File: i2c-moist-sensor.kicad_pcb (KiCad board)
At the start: 2 copper layers, 18 x 149 mm, 25 parts, among them IC1 ATTINY441-SSU, P1 CONN_02X03, X1 16MHz

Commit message: SPBTLE version 1.0 - HW
Only hardware changes
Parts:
- removed C2: 33pp, Capacitors_SMD:C_0603
- removed G***: LOGO, w_logo:Logo_silk_OSHW_6x6mm
- removed G***: LOGO, chirp_logo:ziogas
- removed IC1: ATTINY441-SSU, Housings_SOIC:SOIC-14_3.9x8.7mm_Pitch1.27mm
- removed P1: CONN_02X03, Pin_Headers:Pin_Header_Straight_2x03
- removed the REF** at (91.5, 17.0)
- removed the REF** at (98.5, 17.0)
- removed TH1: NCP18XH103F03RB, Resistors_SMD:R_0603
- removed X1: 16MHz, Crystals:Crystal_HC49-SD_SMD
- added C7: 1u, Capacitors_SMD:C_0603_HandSoldering, B.Cu at (52.2, 32.2)
- added D4: LED, LEDs:LED_0603_HandSoldering, F.Cu at (53.2, 58.7)
- added J1: Conn_02x05_Odd_Even, SBenoit:50mils_JTAG, B.Cu at (57.3, 37.4)
- added J2: Conn_01x02, Pin_Headers:Pin_Header_Straight_1x02_Pitch1.27mm, F.Cu at (57.8, 26.2)
- added Q1: BSS83P, TO_SOT_Packages_SMD:SOT-23_Handsoldering, B.Cu at (57.2, 30.0)
- added Q2: RUC002N05HZGT116CT, TO_SOT_Packages_SMD:SOT-23_Handsoldering, B.Cu at (53.2, 45.5)
- added Q3: RUC002N05HZGT116CT, TO_SOT_Packages_SMD:SOT-23_Handsoldering, B.Cu at (53.4, 61.2)
- added Q4: RUC002N05HZGT116CT, TO_SOT_Packages_SMD:SOT-23_Handsoldering, B.Cu at (53.4, 55.0)
- added R10: 100, Resistors_SMD:R_0603_HandSoldering, B.Cu at (52.5, 49.0)
- added R11: 100, Resistors_SMD:R_0603_HandSoldering, B.Cu at (52.5, 63.8)
- added R12: 100, Resistors_SMD:R_0603_HandSoldering, B.Cu at (52.8, 58.0)
- added R3: 1M, Resistors_SMD:R_0603_HandSoldering, F.Cu at (54.8, 67.0)
- added REF**: MountingHole_3.2mm_M3, Mounting_Holes:MountingHole_3.2mm_M3, F.Cu at (50.5, 27.5)
- added REF**: MountingHole_3.2mm_M3, Mounting_Holes:MountingHole_3.2mm_M3, F.Cu at (65.5, 50.0)
- added SW1: SW_Push, Buttons_Switches_SMD:SW_SPST_EVPBF, F.Cu at (58.0, 53.8)
- added U1: SPBTLE-1S, SBenoit:SPBTLE-1s, F.Cu at (58.8, 36.4)
- C1: value 33p -> 330n; footprint Capacitors_SMD:C_0603 -> Capacitors_SMD:C_0603_HandSoldering; moved to B.Cu
- C3: value 1u -> 1n; footprint Capacitors_SMD:C_0603 -> Capacitors_SMD:C_0603_HandSoldering
- C4: value 1n -> 10n; footprint Capacitors_SMD:C_0603 -> Capacitors_SMD:C_0603_HandSoldering
- C5: footprint Capacitors_SMD:C_0603 -> Capacitors_SMD:C_0603_HandSoldering
- C6: value 1u -> 100n; footprint Capacitors_SMD:C_0603 -> Capacitors_SMD:C_0603_HandSoldering; moved to B.Cu
- D3: footprint LEDs:LED-0603 -> LEDs:LED_0603_HandSoldering
- R1: value 10k -> 1M; footprint Resistors_SMD:R_0603 -> Resistors_SMD:R_0603_HandSoldering
- R2: value 10k 0.1% -> 1M; footprint Resistors_SMD:R_0603 -> Resistors_SMD:R_0603_HandSoldering
- R4, R5, R7, R9: footprint Resistors_SMD:R_0603 -> Resistors_SMD:R_0603_HandSoldering
- R6: value 1M -> 47k; footprint Resistors_SMD:R_0603 -> Resistors_SMD:R_0603_HandSoldering; moved to B.Cu
- R8: value 1M -> 330; footprint Resistors_SMD:R_0603 -> Resistors_SMD:R_0603_HandSoldering
- moved D3 52.9 mm to (51.4, 58.7)
- moved R9 49.6 mm to (52.5, 54.2)
- moved R1 49.1 mm to (54.8, 65.2)
- moved C3 47.0 mm to (54.8, 63.5), turned to 180 degrees
- moved R2 44.5 mm to (52.5, 49.8)
- moved R8 43.0 mm to (52.5, 52.0)
- moved C1 42.2 mm to (54.5, 27.9)
- moved C6 42.2 mm to (52.2, 31.0), turned to 0 degrees
- moved D2 38.9 mm to (58.5, 68.6)
- moved R4 38.9 mm to (52.5, 68.8)
- moved D1 38.9 mm to (55.7, 68.6)
- moved C4 37.9 mm to (55.8, 46.8)
- moved C5 37.5 mm to (59.0, 63.5)
- moved R5 36.4 mm to (59.0, 65.2), turned to 0 degrees
- moved R7 36.4 mm to (59.0, 67.0), turned to 180 degrees
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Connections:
- C1 pad 1: Net-(C1-Pad1) -> +3V0
- C1 pad 2: GND -> Net-(C1-Pad2)
- C3 pad 1: VCC -> /SENSE_LOW
- C4 pad 1: /SENSE_LOW -> /RESET
- C5 pad 1: /MISO/SENSE_HIGH -> /SENSE_HIGH
- C6 pad 1: /RESET -> GND
- C6 pad 2: GND -> VCC
- D2 pad 2: /MISO/SENSE_HIGH -> /SENSE_HIGH
- R1 pad 1: /RESET -> /SENSE_LOW
- R1 pad 2: VCC -> /POWER
- R2 pad 1: Net-(IC1-Pad11) -> +3V0
- R2 pad 2: /THERMISTOR -> Net-(C1-Pad2)
- R5 pad 1: /SENSE_LOW -> /SENSE_HIGH
- R5 pad 2: Net-(IC1-Pad11) -> /POWER
- R6 pad 1: /MISO/SENSE_HIGH -> /RESET
- R6 pad 2: Net-(IC1-Pad11) -> VCC
- R7 pad 2: /SENSE_LOW -> /SENSE_HIGH
- R8 pad 1: GND -> Net-(D3-Pad1)
- R8 pad 2: /MISO/SENSE_HIGH -> VCC
- R9 pad 1: Net-(D3-Pad2) -> Net-(D4-Pad1)
- R9 pad 2: Net-(IC1-Pad12) -> VCC
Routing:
- net GND: track 223.8 -> 108.4 mm, vias 145 -> 78
- net /EXCITATION: track 13.6 -> 127.7 mm, vias 2 -> 63
- net +3V0: track 0.00 -> 59.7 mm, vias 0 -> 2
- net Net-(C1-Pad2): track 0.00 -> 53.4 mm, vias 0 -> 1
- net /POWER: track 0.00 -> 48.5 mm, vias 0 -> 3
- net /SENSE_HIGH: track 0.00 -> 41.7 mm
- net /MISO/SENSE_HIGH: track 38.1 -> 0.00 mm, vias 2 -> 0
- net VCC: track 16.5 -> 52.9 mm
- net /SENSE_LOW: track 11.5 -> 42.9 mm
- net /LED1: track 0.00 -> 31.2 mm, vias 0 -> 1
- net /LED2: track 0.00 -> 27.4 mm, vias 0 -> 1
- net /SCK/SCL: track 23.0 -> 0.00 mm
- net /MOSI/SDA: track 21.7 -> 0.00 mm
- net Net-(IC1-Pad11): track 20.2 -> 0.00 mm, vias 3 -> 0
- net /RESET: track 24.1 -> 11.1 mm, vias 0 -> 1
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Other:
- board size 18 x 149 mm -> 20 x 149 mm
- rule trace_min: 0.254 -> 0.13
- rule via_min_drill: 0.4 -> 0.2
- rule via_min_size: 0.7 -> 0.45
- board text added: "BLE moisture sensor v1"
- board text added: "Originally from : Catnip Electronics http://wemakethings.net/chirp mic@wemakethings.net Modified by : Simon Benoit Gitbuh : Eriobis spiky1987@hotmail.com"
- board text removed: "Catnip Electronics http://wemakethings.net/chirp mic@wemakethings.net"
- board text removed: "GND"
- board text removed: "MISO"
- board text removed: "RESET"
- board text removed: "SCK SCL"
- board text removed: "SDA MOSI"
- board text removed: "Soil moisture sensor v2.7.5"
- board text removed: "VCC"

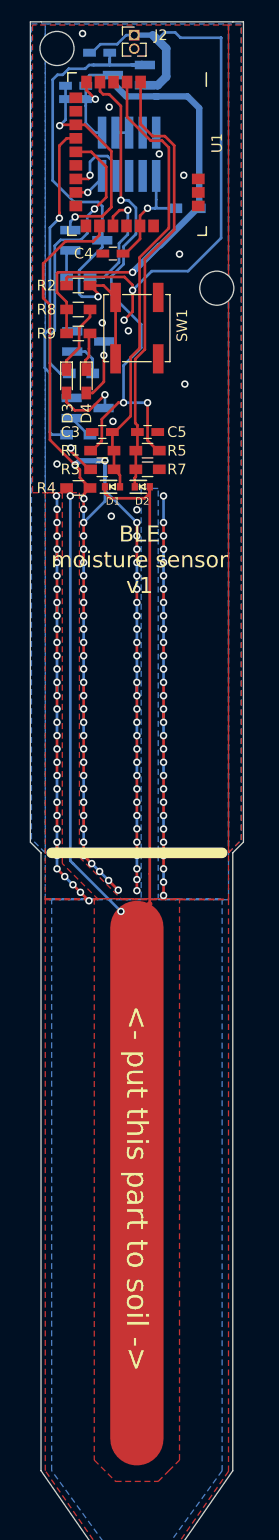
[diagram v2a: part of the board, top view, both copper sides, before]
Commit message: Updated to Rev1
- Naming from 1.0 to Rev version number
- Added pull up for vcc latch
- Added button input
- Removed led2
- Added BOOT pin jumper and pullup
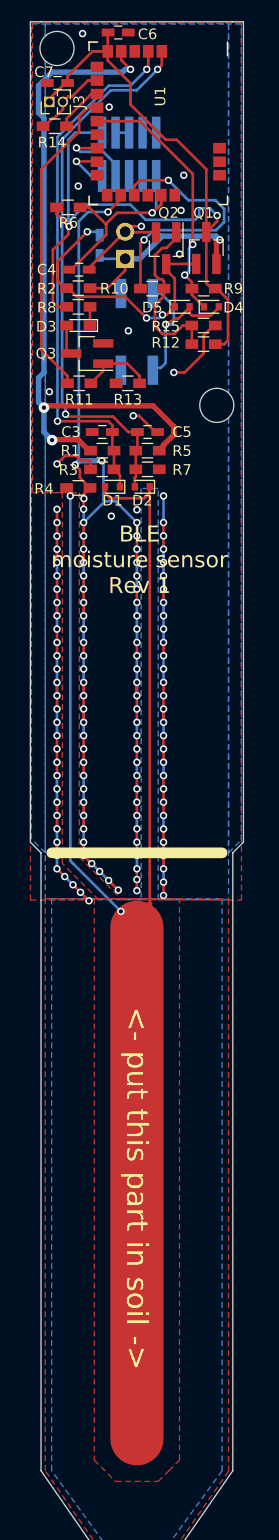
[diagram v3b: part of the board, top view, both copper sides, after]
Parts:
- removed Q4: RUC002N05HZGT116CT, TO_SOT_Packages_SMD:SOT-23_Handsoldering
- added D5: BAT54, Diodes_SMD:D_SOD-523, F.Cu at (62.2, 51.8)
- added J3: Conn_01x02, Pin_Headers:Pin_Header_Straight_1x02_Pitch1.27mm, F.Cu at (49.8, 32.5)
- added R13: 1M, Resistors_SMD:R_0603_HandSoldering, F.Cu at (57.1, 58.9)
- added R14: 47k, Resistors_SMD:R_0603_HandSoldering, F.Cu at (50.3, 34.8)
- added R15: 5M, Resistors_SMD:R_0603_HandSoldering, F.Cu at (64.3, 53.5)
- C6, C7, Q2, Q3, R10, R11, R6: moved to F.Cu
- D1, D2: footprint SMD_Packages:SOD-523 -> Diodes_SMD:D_SOD-523
- D4: value LED -> BAT54; footprint LEDs:LED_0603_HandSoldering -> Diodes_SMD:D_SOD-523
- J2: footprint Pin_Headers:Pin_Header_Straight_1x02_Pitch1.27mm -> Pin_Headers:Pin_Header_Angled_1x02_Pitch2.54mm; moved to B.Cu
- Q1: value BSS83P -> BSS84; moved to F.Cu
- R12: value 100 -> 1M; moved to F.Cu
- R8: value 330 -> 100
- R9: value 330 -> 1M
- SW1: value SW_Push -> SW_SPST; footprint Buttons_Switches_SMD:SW_SPST_EVPBF -> SBenoit:TL3305AF160QG; moved to B.Cu
- moved J2 21.0 mm to (56.9, 47.2)
- moved C1 18.1 mm to (54.5, 46.0), turned to 90 degrees
- moved Q1 17.8 mm to (64.5, 46.2), turned to 90 degrees
- moved D4 13.7 mm to (65.0, 51.8), turned to 0 degrees
- moved R9 12.5 mm to (64.3, 50.0)
- moved R12 11.8 mm to (64.3, 55.2), turned to 180 degrees
- moved R6 11.2 mm to (51.6, 42.4), turned to 180 degrees
- moved REF** 11.0 mm to (65.5, 61.0)
- moved Q2 7.54 mm to (60.8, 46.2), turned to 270 degrees
- moved R10 7.01 mm to (59.4, 50.0)
- moved C6 6.40 mm to (56.2, 26.0), turned to 180 degrees
- moved D3 5.35 mm to (52.5, 53.5), turned to 180 degrees
- moved Q3 5.12 mm to (53.3, 56.1), turned to 180 degrees
- moved R11 4.82 mm to (52.6, 58.9)
- moved C4 3.51 mm to (52.6, 48.3), turned to 0 degrees
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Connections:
- D4 pad 1: Net-(D4-Pad1) -> /BTN_INPUT
- R10 pad 1: /POWER_ON_PIN -> Net-(Q2-Pad1)
- R10 pad 2: Net-(Q2-Pad1) -> /POWER_ON_PIN
- R12 pad 1: /LED2 -> VCC
- R12 pad 2: Net-(Q4-Pad1) -> Net-(Q2-Pad1)
- R9 pad 1: Net-(D4-Pad1) -> VCC
- R9 pad 2: VCC -> /BTN_INPUT
- SW1 pad 1: Net-(C1-Pad2) -> Net-(D4-Pad2)
- U1 pad 10: /LED2 -> /BTN_INPUT
- U1 pad 7: (no net) -> Net-(J3-Pad2)
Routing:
- net +3V0: track 59.7 -> 20.0 mm, vias 2 -> 1
- net VCC: track 52.9 -> 85.6 mm
- net /LED2: track 27.4 -> 0.00 mm, vias 1 -> 0
- net Net-(C1-Pad2): track 53.4 -> 27.1 mm, vias 1 -> 3
- net /BTN_INPUT: track 0.00 -> 24.6 mm, vias 0 -> 2
- net /POWER: track 48.5 -> 65.5 mm
- net Net-(Q2-Pad1): track 2.69 -> 16.6 mm
- net /POWER_ON_PIN: track 11.1 -> 24.8 mm, vias 1 -> 2
- net Net-(D4-Pad2): track 5.98 -> 17.2 mm
- net /SENSE_HIGH: track 41.7 -> 52.3 mm, vias 0 -> 2
- net /RESET: track 11.1 -> 21.5 mm
- net Net-(J3-Pad2): track 0.00 -> 8.26 mm
- net /SENSE_LOW: track 42.9 -> 50.8 mm, vias 0 -> 2
- net Net-(D3-Pad1): track 6.55 -> 1.75 mm
- net Net-(Q3-Pad1): track 2.37 -> 6.91 mm
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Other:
- board text added: "<- put this part in soil ->"
- board text added: "BLE moisture sensor Rev 1"
- board text added: "Hw Info : https://github.com/Eriobis/i2c-moisture-sensor"
- board text removed: "<- put this part to soil ->"
- board text removed: "BLE moisture sensor v1"
